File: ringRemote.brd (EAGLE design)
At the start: 30 x 20 mm, 25 parts, among them J1 AMPHENOL_10118192-0001LFAMPHE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, Y1 32.768kHz

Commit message: misc save
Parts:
- moved J1 50.2 mm to (24.0, 4.00)
- moved Y1 9.06 mm to (23.1, 12.8)
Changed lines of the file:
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@@
 <element name="D1" library="ringRemote" package="LED-0603" value="RED" x="23.37" y="8.86"/>
 <element name="R2" library="ringRemote" package="0201" value="100k" x="27.18" y="10.13"/>
-<element name="Y1" library="ringRemote" package="CRYSTAL-SMD-3.2X1.5MM" value="32.768kHz" x="22.1" y="3.78">
-<attribute name="PROD_ID" value="XTAL-13062" x="22.1" y="3.78" size="1.778" layer="27" display="off"/>
+<element name="Y1" library="ringRemote" package="CRYSTAL-SMD-3.2X1.5MM" value="32.768kHz" x="23.1" y="12.78">
+<attribute name="PROD_ID" value="XTAL-13062" x="23.1" y="12.78" size="1.778" layer="27" display="off"/>
 </element>
 <element name="U$1" library="ringRemote" package="T2044+5C" value="MAX32660" x="5.67" y="3.75"/>
@@
 <attribute name="VERSION" value="v01" x="-16" y="-26" size="1.778" layer="27" display="off"/>
 </element>
-<element name="J1" library="ringRemote" package="AMPHENOL_10118192-0001LF_0" value="AMPHENOL_10118192-0001LFAMPHENOL_10118192-0001LF_0_0" x="-10" y="-33">
-<attribute name="APPROVED_ALTERNATE_PART_NUMBER" value="609-4613-1-ND" x="-10" y="-33" size="1.778" layer="27" display="off"/>
-<attribute name="CENTROID_NOT_SPECIFIED" value="No" x="-10" y="-33" size="1.778" layer="27" display="off"/>
-<attribute name="DATASHEET" value="http://portal.fciconnect.com/Comergent//fci/drawing/10118192.pdf" x="-10" y="-33" size="1.778" layer="27" display="off"/>
-<attribute name="DIGIKEY_DESCRIPTION" value="CONN USB MICRO B RECPT SMT R/A" x="-10" y="-33" size="1.778" layer="27" display="off"/>
-<attribute name="DIGIKEY_PART_NUMBER" value="609-4613-1-ND" x="-10" y="-33" size="1.778" layer="27" display="off"/>
-<attribute name="IS_FEMALE" value="yes" x="-10" y="-33" size="1.778" layer="27" display="off"/>
-<attribute name="LEAD_FREE" value="yes" x="-10" y="-33" size="1.778" layer="27" display="off"/>
-<attribute name="MF" value="Amphenol" x="-10" y="-33" size="1.778" layer="27" display="off"/>
-<attribute name="MOUSER_PART_NUMBER" value="649-10118192-0001LF" x="-10" y="-33" size="1.778" layer="27" display="off"/>
-<attribute name="MPN" value="10118192-0001LF" x="-10" y="-33" size="1.778" layer="27" display="off"/>
-<attribute name="PACKAGE" value="CONN_SMT_7MM86_5MM57_HDMI" x="-10" y="-33" size="1.778" layer="27" display="off"/>
-<attribute name="PREFIX" value="J" x="-10" y="-33" size="1.778" layer="27" display="off"/>
-<attribute name="ROHS" value="yes" x="-10" y="-33" size="1.778" layer="27" display="off"/>
-<attribute name="TEMPERATURE_RANGE_HIGH" value="+80°C" x="-10" y="-33" size="1.778" layer="27" display="off"/>
-<attribute name="TEMPERATURE_RANGE_LOW" value="-30°C" x="-10" y="-33" size="1.778" layer="27" display="off"/>
-<attribute name="VOLTAGE" value="100V" x="-10" y="-33" size="1.778" layer="27" display="off"/>
+<element name="J1" library="ringRemote" package="AMPHENOL_10118192-0001LF_0" value="AMPHENOL_10118192-0001LFAMPHENOL_10118192-0001LF_0_0" x="24" y="4">
+<attribute name="APPROVED_ALTERNATE_PART_NUMBER" value="609-4613-1-ND" x="24" y="4" size="1.778" layer="27" display="off"/>
+<attribute name="CENTROID_NOT_SPECIFIED" value="No" x="24" y="4" size="1.778" layer="27" display="off"/>
+<attribute name="DATASHEET" value="http://portal.fciconnect.com/Comergent//fci/drawing/10118192.pdf" x="24" y="4" size="1.778" layer="27" display="off"/>
+<attribute name="DIGIKEY_DESCRIPTION" value="CONN USB MICRO B RECPT SMT R/A" x="24" y="4" size="1.778" layer="27" display="off"/>
+<attribute name="DIGIKEY_PART_NUMBER" value="609-4613-1-ND" x="24" y="4" size="1.778" layer="27" display="off"/>
+<attribute name="IS_FEMALE" value="yes" x="24" y="4" size="1.778" layer="27" display="off"/>
+<attribute name="LEAD_FREE" value="yes" x="24" y="4" size="1.778" layer="27" display="off"/>
+<attribute name="MF" value="Amphenol" x="24" y="4" size="1.778" layer="27" display="off"/>
+<attribute name="MOUSER_PART_NUMBER" value="649-10118192-0001LF" x="24" y="4" size="1.778" layer="27" display="off"/>
+<attribute name="MPN" value="10118192-0001LF" x="24" y="4" size="1.778" layer="27" display="off"/>
+<attribute name="PACKAGE" value="CONN_SMT_7MM86_5MM57_HDMI" x="24" y="4" size="1.778" layer="27" display="off"/>
+<attribute name="PREFIX" value="J" x="24" y="4" size="1.778" layer="27" display="off"/>
+<attribute name="ROHS" value="yes" x="24" y="4" size="1.778" layer="27" display="off"/>
+<attribute name="TEMPERATURE_RANGE_HIGH" value="+80°C" x="24" y="4" size="1.778" layer="27" display="off"/>
+<attribute name="TEMPERATURE_RANGE_LOW" value="-30°C" x="24" y="4" size="1.778" layer="27" display="off"/>
+<attribute name="VOLTAGE" value="100V" x="24" y="4" size="1.778" layer="27" display="off"/>
 </element>
 </elements>
@@
 <contactref element="U$2" pad="P$34"/>
 <wire x1="9.0225" y1="8.4845" x2="12.51" y2="12.105" width="0" layer="19" extent="1-1"/>
-<wire x1="23.35" y1="3.78" x2="9.0225" y2="8.4845" width="0" layer="19" extent="1-1"/>
+<wire x1="24.35" y1="12.78" x2="9.0225" y2="8.4845" width="0" layer="19" extent="1-1"/>
 </signal>
 <signal name="CLKSRC">
@@
 <contactref element="U$2" pad="P$33"/>
 <wire x1="8.4125" y1="8.4845" x2="12.51" y2="8.295" width="0" layer="19" extent="1-1"/>
-<wire x1="20.85" y1="3.78" x2="8.4125" y2="8.4845" width="0" layer="19" extent="1-1"/>
+<wire x1="21.85" y1="12.78" x2="8.4125" y2="8.4845" width="0" layer="19" extent="1-1"/>
 </signal>
 <signal name="N$1">
@@
 <contactref element="J1" pad="8"/>
 <contactref element="J1" pad="7"/>
-<wire x1="-11.2" y1="-33.115" x2="-13.8" y2="-33.115" width="0" layer="19" extent="1-1"/>
-<wire x1="-8.8" y1="-33.115" x2="-11.2" y2="-33.115" width="0" layer="19" extent="1-1"/>
-<wire x1="-6.2" y1="-33.115" x2="-8.8" y2="-33.115" width="0" layer="19" extent="1-1"/>
-<wire x1="-13.1" y1="-30.565" x2="-13.8" y2="-33.115" width="0" layer="19" extent="1-1"/>
-<wire x1="-6.9" y1="-30.565" x2="-6.2" y2="-33.115" width="0" layer="19" extent="1-1"/>
-<wire x1="-8.7" y1="-30.44" x2="-6.9" y2="-30.565" width="0" layer="19" extent="1-1"/>
-<wire x1="-14" y1="-14.275" x2="-13.1" y2="-30.565" width="0" layer="19" extent="1-1"/>
+<wire x1="22.8" y1="3.885" x2="20.2" y2="3.885" width="0" layer="19" extent="1-1"/>
+<wire x1="25.2" y1="3.885" x2="22.8" y2="3.885" width="0" layer="19" extent="1-1"/>
+<wire x1="27.8" y1="3.885" x2="25.2" y2="3.885" width="0" layer="19" extent="1-1"/>
+<wire x1="20.9" y1="6.435" x2="20.2" y2="3.885" width="0" layer="19" extent="1-1"/>
+<wire x1="27.1" y1="6.435" x2="27.8" y2="3.885" width="0" layer="19" extent="1-1"/>
+<wire x1="25.3" y1="6.56" x2="27.1" y2="6.435" width="0" layer="19" extent="1-1"/>
+<wire x1="-14" y1="-14.275" x2="20.9" y2="6.435" width="0" layer="19" extent="1-1"/>
 <wire x1="-13.75" y1="-7.95" x2="-14" y2="-14.275" width="0" layer="19" extent="1-1"/>
 <wire x1="-3" y1="-4.35" x2="-13.75" y2="-7.95" width="0" layer="19" extent="1-1"/>
@@
 <contactref element="C7" pad="1"/>
 <contactref element="J1" pad="1"/>
-<wire x1="-14" y1="-13.725" x2="-11.3" y2="-30.44" width="0" layer="19" extent="1-1"/>
+<wire x1="-14" y1="-13.725" x2="22.7" y2="6.56" width="0" layer="19" extent="1-1"/>
 <wire x1="-3.95" y1="-4.35" x2="-14" y2="-13.725" width="0" layer="19" extent="1-1"/>
 <wire x1="-2.05" y1="-4.35" x2="-3.95" y2="-4.35" width="0" layer="19" extent="1-1"/>

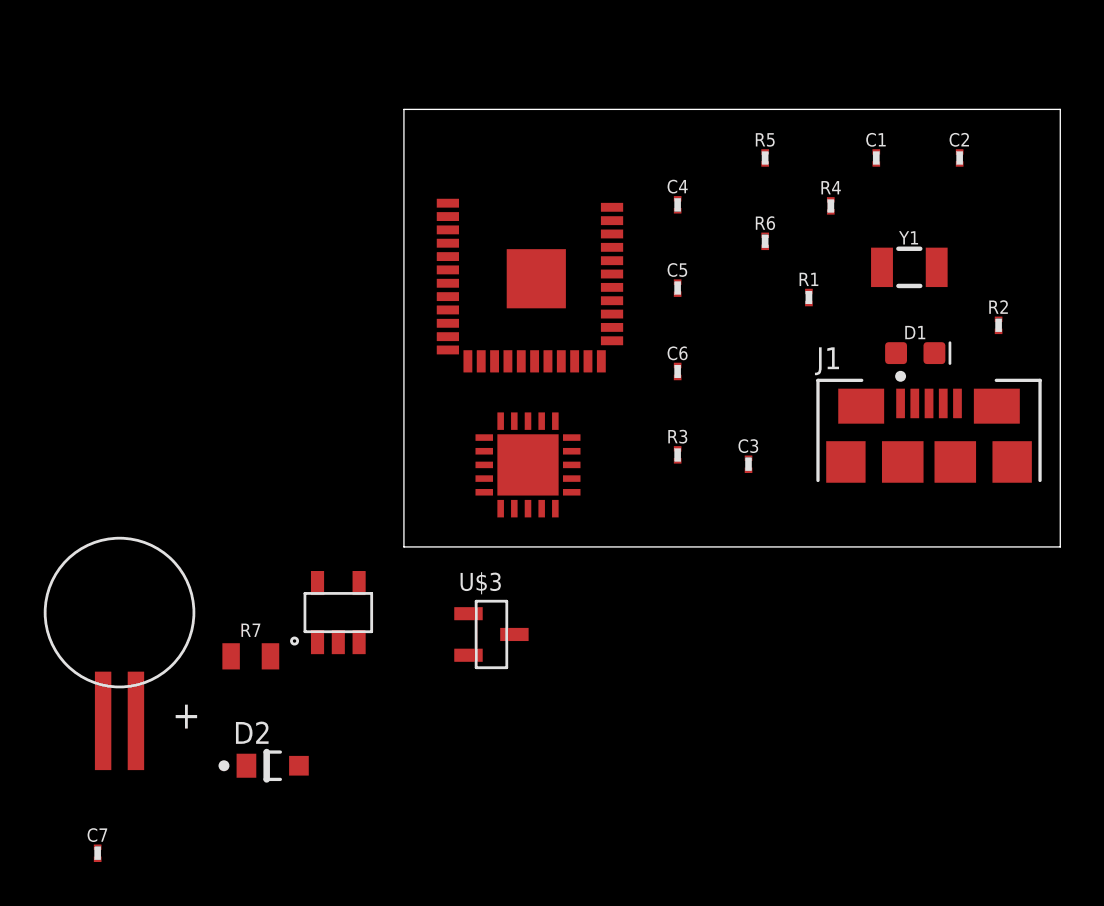
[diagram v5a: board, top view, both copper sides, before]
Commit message: made rough layout of board; swapped some pins for pushbuttons in sch (to atbtlc); understood programming workflow a bit better (likely using SWD instead of i2c)
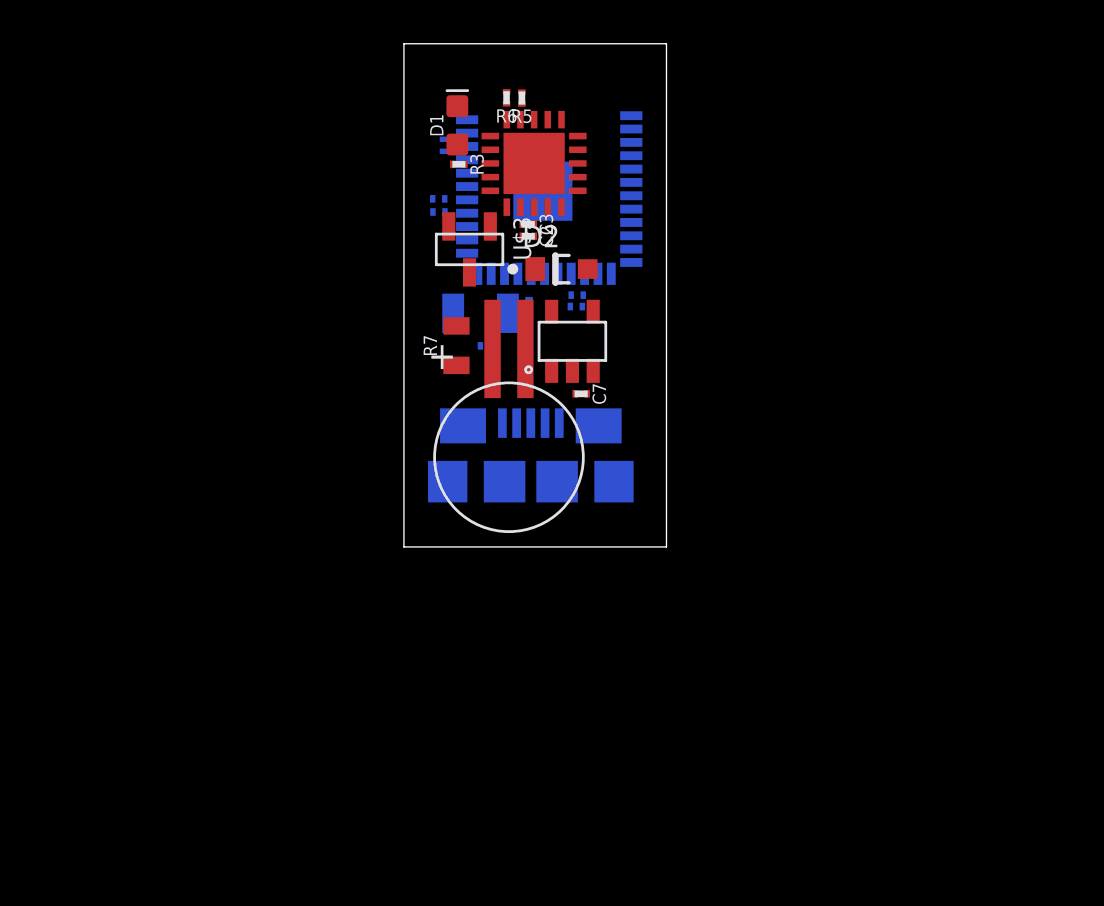
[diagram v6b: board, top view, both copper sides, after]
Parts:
- moved C7 30.5 mm to (8.10, 7.00), turned to 270 degrees
- moved D2 26.3 mm to (7.20, 12.7)
- moved D1 23.4 mm to (2.44, 19.3), turned to 90 degrees
- moved R2 21.5 mm to (5.72, 11.0), flipped to the bottom
- moved C2 20.0 mm to (5.68, 14.2), turned to 270 degrees
- moved Y1 19.7 mm to (3.50, 10.7), flipped to the bottom
- moved U$5 19.2 mm to (4.80, 4.10), turned to 180 degrees
- moved FRAME2 18.5 mm to (-5.80, -10.6)
- moved J1 18.2 mm to (5.80, 3.10), flipped to the bottom
- moved R4 17.9 mm to (1.59, 15.9), flipped to the bottom, turned to 90 degrees
- moved U$3 17.6 mm to (3.00, 13.6), turned to 270 degrees
- moved R1 17.4 mm to (1.60, 15.3), flipped to the bottom, turned to 90 degrees
- moved R7 17.0 mm to (2.40, 9.20), turned to 90 degrees
- moved R3 16.6 mm to (2.51, 17.5), turned to 270 degrees
- moved U$4 16.4 mm to (7.70, 9.40)
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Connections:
- net N$8 renamed PB3
- net N$9 renamed PB4
- removed net N$6: R4.1, U$1.P$12
- removed net N$7: R1.1, U$1.P$11
- new net I2C0_SCL: U$1.P$12
- new net I2C0_SDA: U$1.P$11
- new net PB1: R1.1, U$2.P$4
- new net PB2: R4.1, U$2.P$5
- new net SWDCLK: U$1.P$1
- new net SWDIO: U$1.P$2
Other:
- board size 30 x 20 mm -> 12 x 23 mm

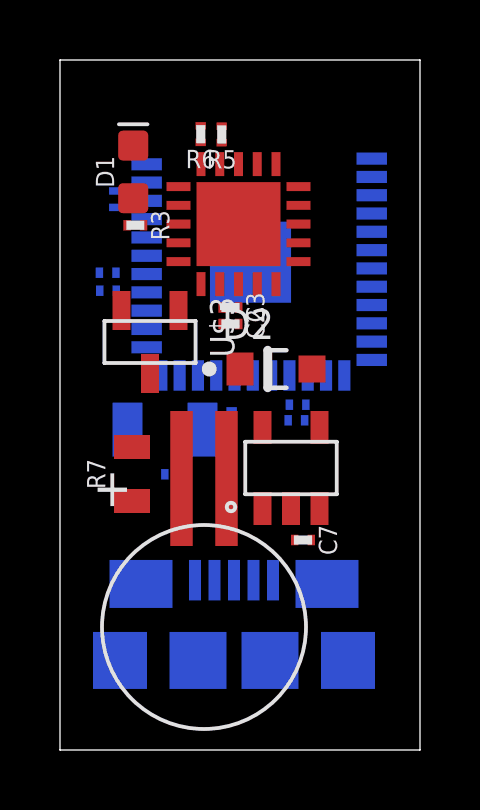
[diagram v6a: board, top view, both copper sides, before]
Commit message: think I moved the pb's back to MAX32660 (using the i2c lines because they're not needed)
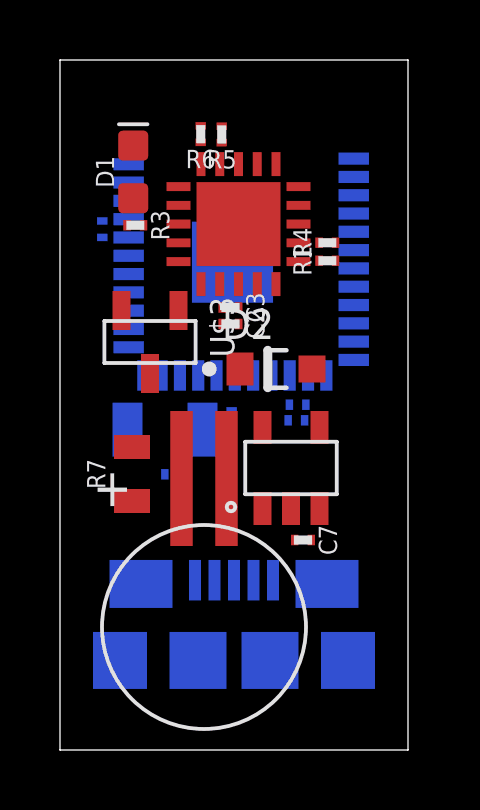
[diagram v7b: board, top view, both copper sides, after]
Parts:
- moved R4 7.39 mm to (8.91, 16.9), flipped to the top
- moved R1 7.38 mm to (8.91, 16.3), flipped to the top
- moved C4 1.08 mm to (1.41, 17.4)
- moved U$2 0.60 mm to (5.75, 16.3)
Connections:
- removed net I2C0_SCL: U$1.P$12
- removed net I2C0_SDA: U$1.P$11
- net PB1: now also U$1.P$11; no longer U$2.P$4
- net PB2: now also U$1.P$12; no longer U$2.P$5
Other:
- board size 12 x 23 mm -> 11.6 x 23 mm

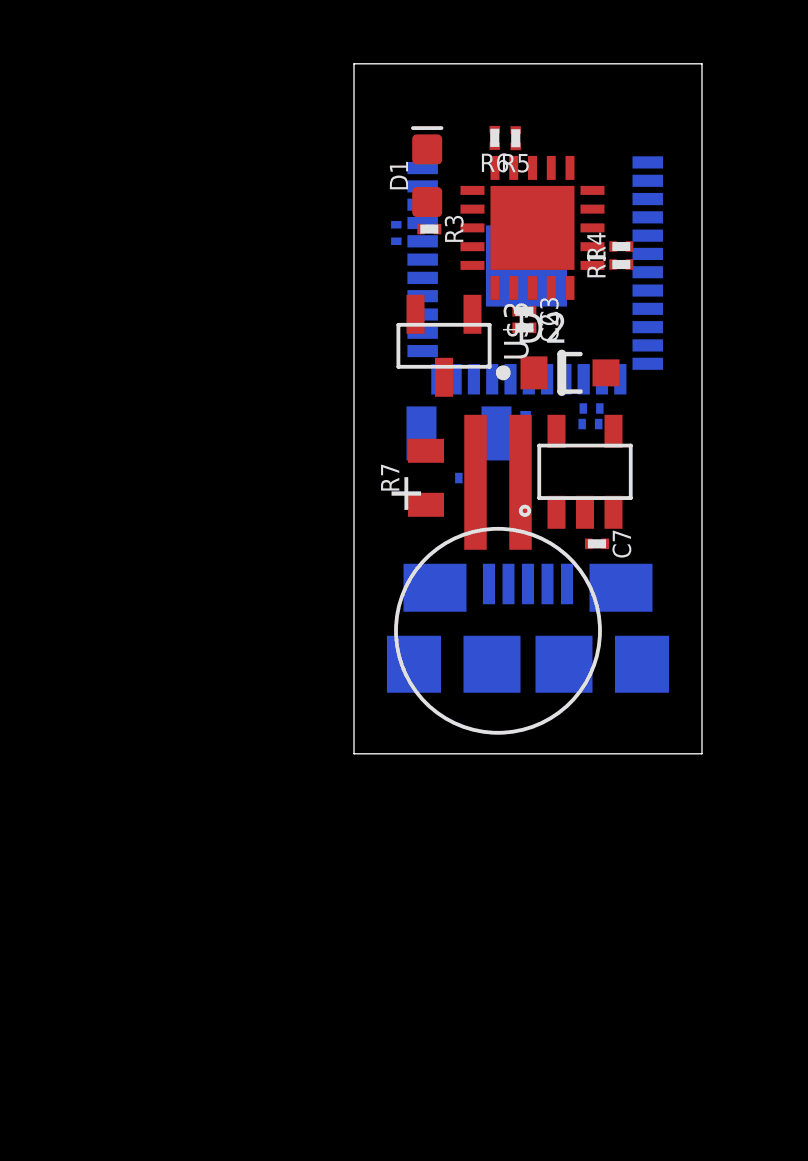
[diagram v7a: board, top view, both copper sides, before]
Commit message: pretty much finished the board; swapped diode out for a smaller package
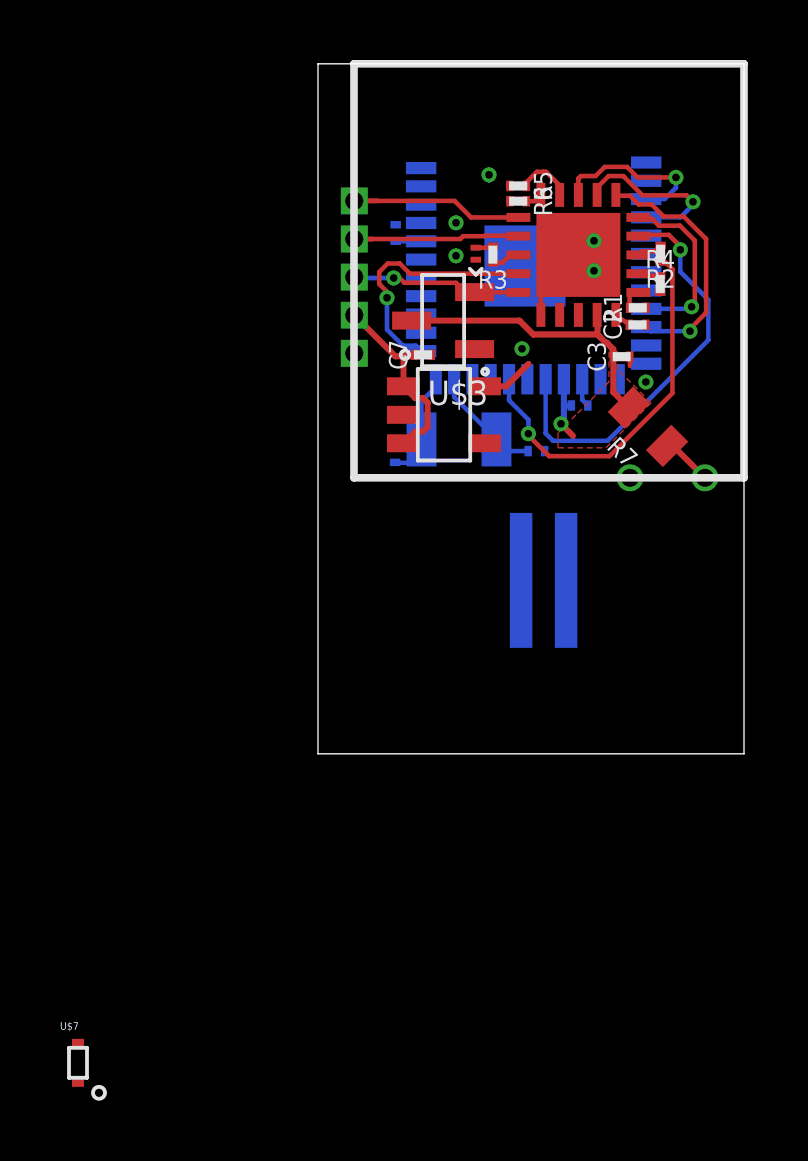
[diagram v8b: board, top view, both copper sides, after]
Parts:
- removed D2: PANASONIC_DB2J31400LPANASONIC_DB2J31400L_0_0, ringRemote:PANASONIC_DB2J31400L_0
- removed J1: AMPHENOL_10118192-0001LFAMPHENOL_10118192-0001LF_0_0, ringRemote:AMPHENOL_10118192-0001LF_0
- added U$6: 1X5_1.27MM, ringRemote:1X5_1.27MM
- added U$7: DB2731400L, ringRemote:SSSMINI2
- D1: value RED -> ORANGE; device ringRemote:LED-0603 -> ringRemote:LED-0201
- moved C7 8.56 mm to (2.30, 13.3), turned to 90 degrees
- moved R7 7.59 mm to (9.80, 10.9), turned to 135 degrees
- moved R2 7.22 mm to (10.2, 16.7), flipped to the top, turned to 180 degrees
- moved U$4 5.07 mm to (3.00, 11.3), turned to 270 degrees
- moved C2 3.77 mm to (9.45, 14.3), turned to 90 degrees
- moved U$5 3.61 mm to (6.32, 0.83), flipped to the bottom
- moved C3 3.57 mm to (8.92, 13.2), turned to 90 degrees
- moved D1 3.06 mm to (4.06, 16.7), turned to 270 degrees
- moved C5 2.53 mm to (1.37, 9.99), turned to 180 degrees
- moved R3 2.28 mm to (4.63, 16.6), turned to 180 degrees
- moved R6 2.25 mm to (5.47, 18.4), turned to 270 degrees
- moved C6 2.01 mm to (6.08, 10.1)
- moved R4 1.80 mm to (10.2, 15.7), turned to 0 degrees
- moved U$1 1.78 mm to (7.48, 16.6)
- moved R5 1.59 mm to (5.47, 18.9), turned to 270 degrees
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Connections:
- removed net D+: J1.3
- removed net D-: J1.2
- removed net VUSB: C7.1, J1.1, U$4.P$1, U$4.P$3
- new net VEXT: C7.1, U$4.P$1, U$4.P$3, U$6.P$2
- net GND: now also U$6.P$1; no longer J1.10, J1.11, J1.5, J1.6, J1.7, J1.8, J1.9
- net MAXRST: now also U$6.P$3
- net N$10: now also U$7.P$2; no longer D2.2
- net SWDCLK: now also U$6.P$5
- net SWDIO: now also U$6.P$4
- net VCC: now also U$7.P$1; no longer D2.1
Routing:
- net VCC: track 0.00 -> 20.8 mm, vias 0 -> 1
- net WAKEMONITOR: track 0.00 -> 13.8 mm, vias 0 -> 1
- net N$4: track 0.00 -> 12.7 mm, vias 0 -> 1
- net BT_RTS: track 0.00 -> 8.43 mm, vias 0 -> 1
- net AO_GPIO_0_WAKE: track 0.00 -> 8.36 mm, vias 0 -> 1
- net SWDCLK: track 0.00 -> 6.49 mm
- net VEXT: track 0.00 -> 6.47 mm
- net SWDIO: track 0.00 -> 6.11 mm
- net BT_CTS: track 0.00 -> 5.99 mm, vias 0 -> 1
- net MAXRST: track 0.00 -> 5.94 mm, vias 0 -> 1
- net BT_TXD: track 0.00 -> 5.79 mm, vias 0 -> 1
- net BT_RXD: track 0.00 -> 5.60 mm, vias 0 -> 1
- net GND: track 0.00 -> 4.75 mm, vias 0 -> 8
- net CLKSRC: track 0.00 -> 4.52 mm
- net N$2: track 0.00 -> 3.78 mm
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- added copper zone on layer 1, net GND
- added copper zone on layer 16, net GND
- added copper zone on layer 1, net VCC
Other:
- board size 11.6 x 23 mm -> 14.2 x 23 mm
